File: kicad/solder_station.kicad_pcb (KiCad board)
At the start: 2 copper layers, 25 parts, among them CON1 AVR-ISP-6, IC1 ATMEGA8-P, P1 Weller Connector, Q1 BS170, Q2 IRF4905, U1 LM7805, U2 LM2902N

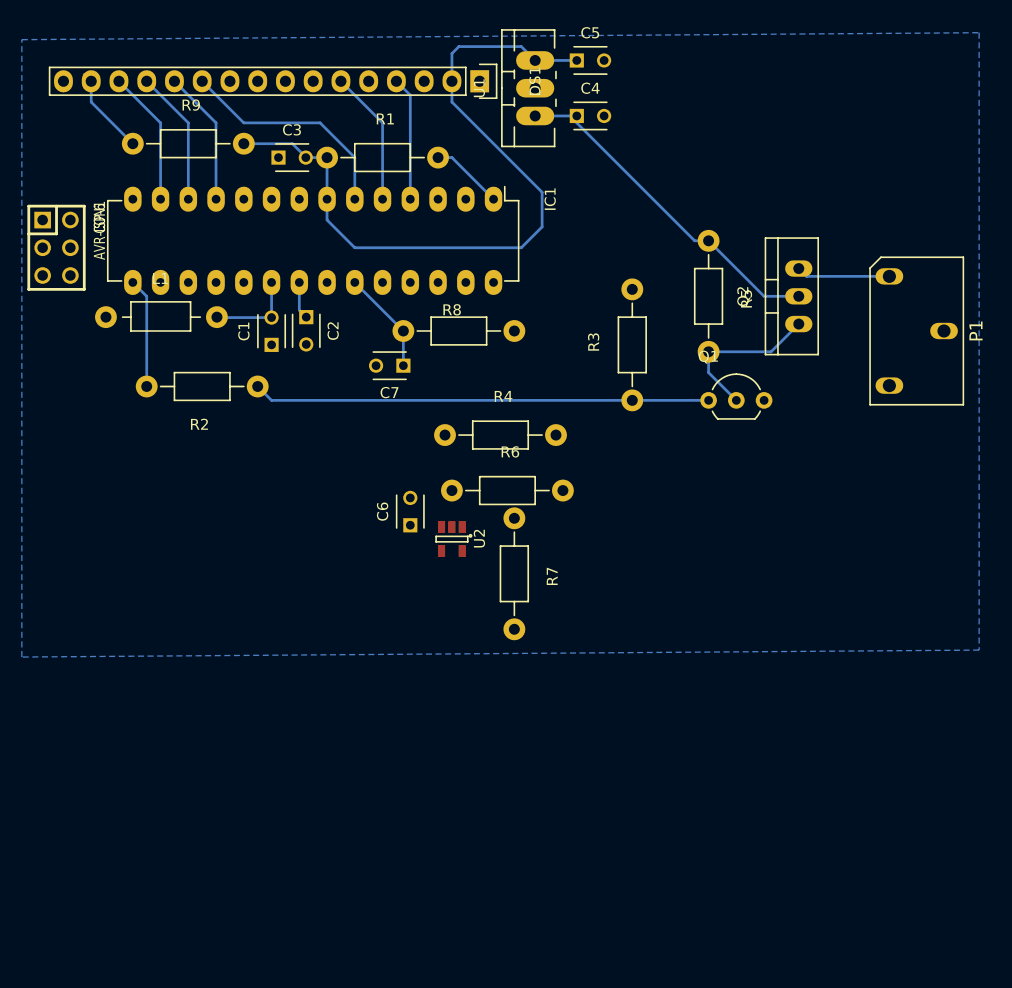
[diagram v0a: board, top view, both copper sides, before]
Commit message: [Kicad] First (bad) version of the PCB.
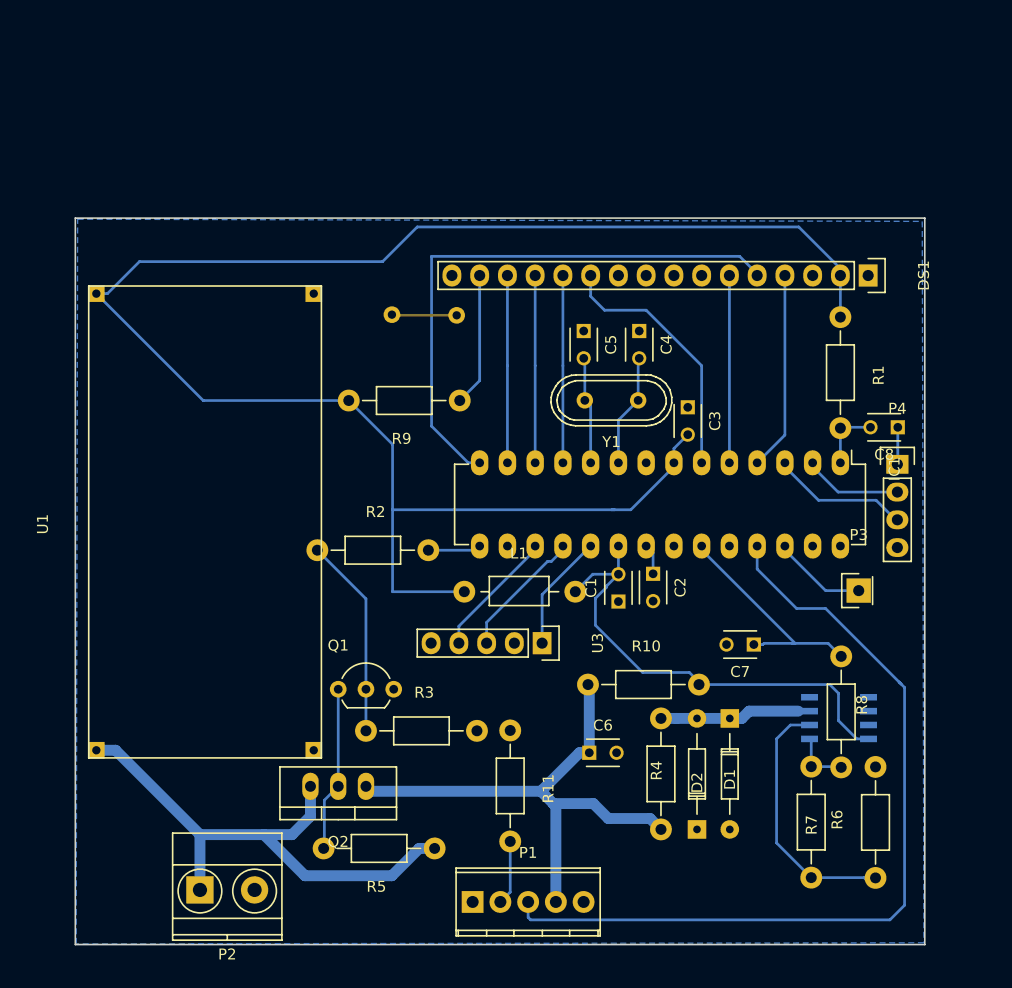
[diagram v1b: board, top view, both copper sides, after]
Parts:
- removed CON1: AVR-ISP-6, connector:CONNECTOR 3 2
- added C8: 100nF, Capacitors_ThroughHole:C_Disc_D3_P2.5, F.Cu at (165.9, 83.1)
- added D1: D, Diodes_ThroughHole:Diode_DO-35_SOD27_Horizontal_RM10, F.Cu at (150.5, 109.8)
- added D2: D, Diodes_ThroughHole:Diode_DO-35_SOD27_Horizontal_RM10, F.Cu at (147.5, 119.9)
- added P2: CONN_01X02, Terminal_Blocks:TerminalBlock_Pheonix_MKDS1.5-2pol, F.Cu at (102.0, 125.5)
- added P3: Standby, Socket_Strips:Socket_Strip_Straight_1x01, F.Cu at (162.3, 98.1)
- added P4: UART, Pin_Headers:Pin_Header_Straight_1x04, F.Cu at (165.9, 86.5)
- added R10: 1MΩ, Resistors_ThroughHole:Resistor_Horizontal_RM10mm, F.Cu at (142.6, 106.7)
- added R11: 1MΩ, Resistors_ThroughHole:Resistor_Horizontal_RM10mm, F.Cu at (130.4, 115.9)
- added REF**1: Pad, my_footprints:Pad, F.Cu at (119.6, 72.8)
- added REF**2: Pad, my_footprints:Pad, F.Cu at (125.5, 72.9)
- added U3: EC11, Pin_Headers:Pin_Header_Straight_1x05, F.Cu at (133.3, 102.9)
- added Y1: 16MHz, Crystals:Crystal_HC49-U_Vertical, F.Cu at (139.7, 80.6)
- C4, C5: value 100nF -> 22pF
- IC1: value ATMEGA8-P -> ATMEGA328-P
- L1: value 10uH -> 10µH
- P1: value Weller Connector -> CONN_01X05; footprint my_footprints:ZIP-3 -> Terminal_Blocks:TerminalBlock_Pheonix_MPT-2.54mm_5pol
- Q1: value BS170 -> 2N7000
- R4: value 1kΩ -> 6.7kΩ
- R5: value R -> 10kΩ
- U1: value LM7805 -> LM2596_module; footprint TO_SOT_Packages_THT:TO-220_Neutral123_Vertical_LargePads -> my_footprints:LM2596
- U2: value LM2902N -> AD8572; footprint TO_SOT_Packages_SMD:SOT-23-5 -> Housings_SOIC:SOIC-8_3.9x4.9mm_Pitch1.27mm; moved to B.Cu
- moved U1 73.7 mm to (91.8, 113.4)
- moved P1 66.2 mm to (127.0, 126.6), turned to 0 degrees
- moved Q2 61.6 mm to (114.7, 116.0), turned to 180 degrees
- moved R5 58.9 mm to (118.4, 121.7), turned to 180 degrees
- moved R8 49.4 mm to (160.7, 109.2), turned to 270 degrees
- moved R1 46.3 mm to (160.7, 78.1), turned to 270 degrees
- moved R6 45.4 mm to (163.9, 119.3), turned to 90 degrees
- moved C3 43.9 mm to (146.7, 81.3), turned to 270 degrees
- moved Q1 43.0 mm to (114.7, 107.1)
- moved L1 41.3 mm to (131.2, 98.2)
- moved C7 41.0 mm to (152.7, 103.0)
- moved R3 40.3 mm to (122.3, 110.9), turned to 0 degrees
- moved IC1 39.9 mm to (160.7, 86.4)
- moved DS1 39.8 mm to (163.2, 69.2)
- moved C1 39.5 mm to (140.3, 99.1)
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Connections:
- net Heater renamed /Heater_PWM
- net LCD_D4 renamed /LCD_D4
- net LCD_D5 renamed /LCD_D5
- net LCD_D6 renamed /LCD_D6
- net LCD_D7 renamed /LCD_D7
- net LCD_RS renamed /LCD_RS
- net LDC_E renamed /LCD_E
- net RESET renamed Net-(C8-Pad2)
- net Temp_sens renamed /Temp_sense
- C4 pad 1: +12V -> GND
- C4 pad 2: GND -> Net-(C4-Pad2)
- C5 pad 1: +5V -> GND
- C5 pad 2: GND -> Net-(C5-Pad2)
- C6 pad 1: Net-(C6-Pad1) -> /Heater+
- DS1 pad 5: GND -> /LCD_RW
- IC1 pad 10: Net-(IC1-Pad10) -> Net-(C5-Pad2)
- IC1 pad 14: Net-(IC1-Pad14) -> /LCD_RW
- IC1 pad 17: MOSI -> /Button_push
- IC1 pad 18: MISO -> /Rotary_B
- IC1 pad 19: SCK -> /Rotary_A
- IC1 pad 2: Net-(IC1-Pad2) -> /RX
- IC1 pad 25: Net-(IC1-Pad25) -> /Button_connected
- IC1 pad 3: Net-(IC1-Pad3) -> /TX
- IC1 pad 9: Net-(IC1-Pad9) -> Net-(C4-Pad2)
- P1 pad 1: Heater_vcc -> GND
- P1 pad 2: Heater_sense -> /Tip
- P1 pad 3: GND -> /Button_connected
- Q2 pad 1: Net-(Q1-Pad2) -> /Heater+
- Q2 pad 2: +12V -> Net-(Q1-Pad1)
- Q2 pad 3: Heater_vcc -> +24V
- R2 pad 1: Net-(Q1-Pad1) -> Net-(Q1-Pad2)
- R3 pad 1: Net-(Q1-Pad1) -> Net-(Q1-Pad2)
- R4 pad 1: Net-(C6-Pad1) -> Net-(D1-Pad1)
- R4 pad 2: Heater_sense -> /Heater+
- R5 pad 1: +12V -> +24V
- R5 pad 2: Net-(Q1-Pad2) -> Net-(Q1-Pad1)
- U1 pad 1: +12V -> +24V
- U2 pad 3: Net-(C6-Pad1) -> Net-(D1-Pad1)
- U2 pad 4: AVcc -> GND
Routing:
- net +5V: track 66.9 -> 161.0 mm
- net /Button_connected: track 0.00 -> 77.2 mm
- net /LCD_RW: track 0.00 -> 52.0 mm
- net /Heater+: track 0.00 -> 50.7 mm
- net +24V: track 0.00 -> 49.5 mm
- net AVcc: track 8.23 -> 44.4 mm
- net +12V: track 31.3 -> 0.00 mm
- net Net-(Q1-Pad1): track 41.8 -> 15.1 mm
- net Net-(R6-Pad1): track 0.00 -> 22.9 mm
- net Net-(D1-Pad1): track 0.00 -> 13.9 mm
- net /TX: track 0.00 -> 12.7 mm
- net /Rotary_B: track 0.00 -> 12.0 mm
- net /Temp_sense: track 9.46 -> 21.3 mm
- net /Button_push: track 0.00 -> 11.8 mm
- net /Rotary_A: track 0.00 -> 11.6 mm
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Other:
- board outline added: 77.8 x 66.5 mm
- net class Default: via_dia 0.6 -> 1.2; via_drill 0.4 -> 0.8
- net class Power added: clearance 0.2, trace_width 1, via_dia 0.6, via_drill 0.4

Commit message: [Kicad] Fix bug in schematics (VGS too high). Still not sure if it is okay this way.
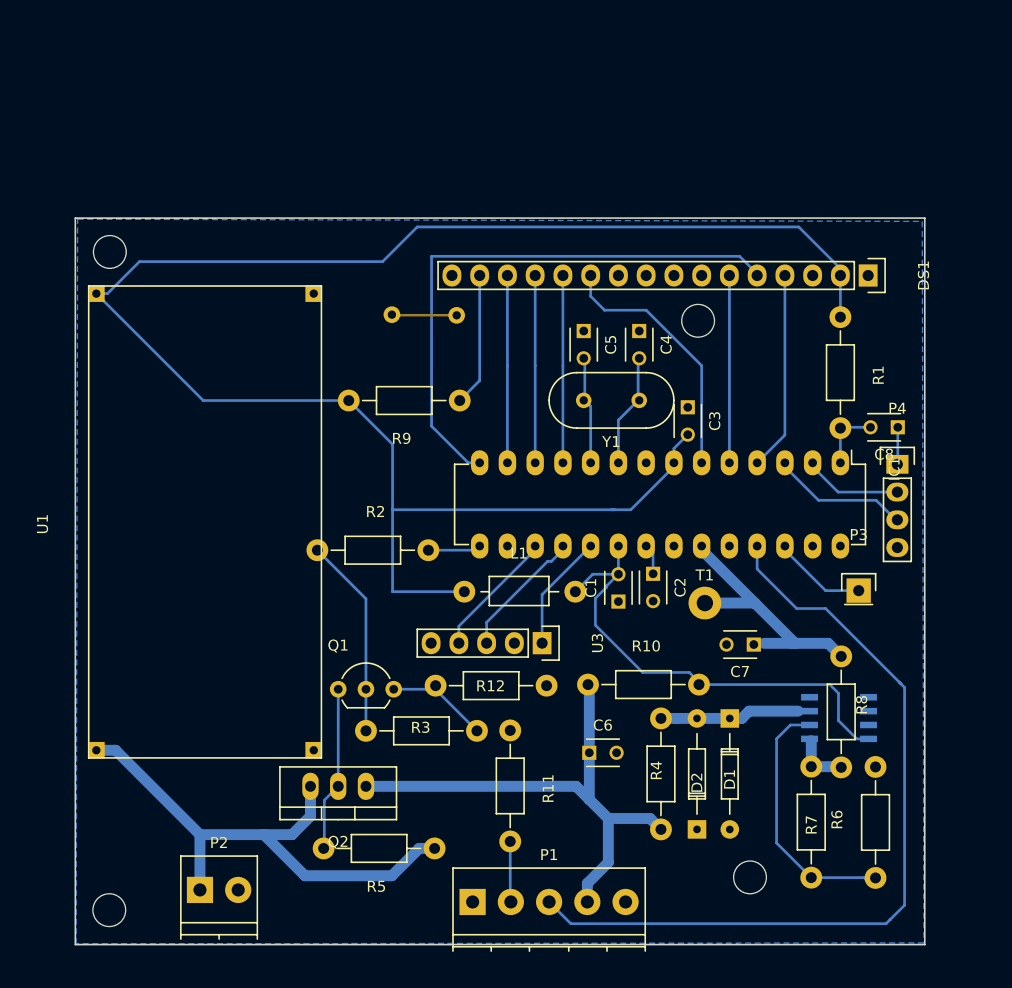
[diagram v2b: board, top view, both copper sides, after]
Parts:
- added Hole1: MountingHole_3mm, Mounting_Holes:MountingHole_3mm, F.Cu at (152.4, 124.3)
- added Hole2: MountingHole_3mm, Mounting_Holes:MountingHole_3mm, F.Cu at (93.7, 127.3)
- added Hole3: MountingHole_3mm, Mounting_Holes:MountingHole_3mm, F.Cu at (93.8, 67.1)
- added Hole4: MountingHole_3mm, Mounting_Holes:MountingHole_3mm, F.Cu at (147.6, 73.4)
- added R12: 10kΩ, Resistors_ThroughHole:Resistor_Horizontal_RM10mm, F.Cu at (128.7, 106.8)
- added T1: Measurement_Point_Round-TH_Big, Measurement_Points:Measurement_Point_Round-TH_Big, F.Cu at (148.2, 99.2)
- P1: footprint Terminal_Blocks:TerminalBlock_Pheonix_MPT-2.54mm_5pol -> Terminal_Blocks:TerminalBlock_Pheonix_PT-3.5mm_5pol
- P2: footprint Terminal_Blocks:TerminalBlock_Pheonix_MKDS1.5-2pol -> Terminal_Blocks:TerminalBlock_Pheonix_PT-3.5mm_2pol
- P3: footprint Socket_Strips:Socket_Strip_Straight_1x01 -> Pin_Headers:Pin_Header_Straight_1x01
- Y1: footprint Crystals:Crystal_HC49-U_Vertical -> Crystals:HC-49V
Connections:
- Q1 pad 3: GND -> Net-(Q1-Pad3)
- R3 pad 2: GND -> Net-(Q1-Pad3)
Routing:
- net Net-(Q1-Pad3): track 0.00 -> 9.67 mm
- net /Temp_sense: track 21.3 -> 26.0 mm
- net /Button_connected: track 77.2 -> 74.8 mm
- net /Heater+: track 50.7 -> 48.5 mm

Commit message: [Kicad] Update schematics. Using ad8551.
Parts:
- removed Hole4: MountingHole_3mm, Mounting_Holes:MountingHole_3mm
- removed T1: Measurement_Point_Round-TH_Big, Measurement_Points:Measurement_Point_Round-TH_Big
- added C9: CP, Capacitors_ThroughHole:C_Radial_D5_L11_P2.5, F.Cu at (112.7, 117.2)
- R10: value 1MΩ -> 300kΩ
- R12, R5: value 10kΩ -> 1kΩ
- R6: value 100Ω -> 1kΩ
- R7: value 50kΩ -> 100kΩ
- moved Q1 16.6 mm to (131.1, 105.2), turned to 180 degrees
- moved Hole3 16.0 mm to (109.7, 67.2)
- moved P2 15.6 mm to (117.5, 123.1)
- moved R6 15.5 mm to (149.0, 114.9), turned to 0 degrees
- moved U2 14.4 mm to (146.8, 105.5)
- moved Hole2 14.1 mm to (107.6, 124.8)
- moved U1 14.1 mm to (105.9, 112.5)
- moved Q2 13.7 mm to (128.2, 114.0), turned to 90 degrees
- moved Hole1 12.9 mm to (165.3, 124.8)
- moved D2 12.1 mm to (153.9, 109.6), turned to 180 degrees
- moved R3 11.8 mm to (111.7, 105.7), turned to 270 degrees
- moved R8 11.1 mm to (152.3, 102.0)
- moved R12 9.33 mm to (121.1, 112.2), turned to 90 degrees
- moved R5 8.76 mm to (118.3, 112.9), turned to 270 degrees
- moved R7 8.24 mm to (156.8, 111.1)
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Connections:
- DS1 pad 10: Net-(DS1-Pad10) -> (no net)
- DS1 pad 7: Net-(DS1-Pad7) -> (no net)
- DS1 pad 8: Net-(DS1-Pad8) -> (no net)
- DS1 pad 9: Net-(DS1-Pad9) -> (no net)
- IC1 pad 16: Net-(IC1-Pad16) -> /Button_push
- IC1 pad 17: /Button_push -> /Rotary_B
- IC1 pad 18: /Rotary_B -> (no net)
- IC1 pad 24: Net-(IC1-Pad24) -> (no net)
- IC1 pad 27: Net-(IC1-Pad27) -> (no net)
- IC1 pad 28: Net-(IC1-Pad28) -> (no net)
- Q1 pad 1: Net-(Q1-Pad1) -> GND
- Q2 pad 1: /Heater+ -> Net-(Q2-Pad1)
- Q2 pad 2: Net-(Q1-Pad1) -> /Heater+
- R12 pad 1: Net-(Q1-Pad3) -> Net-(Q2-Pad1)
- R12 pad 2: GND -> Net-(Q1-Pad3)
- R3 pad 2: Net-(Q1-Pad3) -> GND
- R5 pad 2: Net-(Q1-Pad1) -> Net-(Q2-Pad1)
- U2 pad 1: Net-(R7-Pad1) -> (no net)
- U2 pad 6: (no net) -> Net-(R7-Pad1)
- U2 pad 7: (no net) -> AVcc
- U2 pad 8: AVcc -> (no net)
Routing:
- net /Heater+: track 48.5 -> 25.1 mm
- net +5V: track 161.0 -> 143.6 mm
- net Net-(Q1-Pad1): track 15.1 -> 0.00 mm
- net /Temp_sense: track 26.0 -> 12.1 mm
- net AVcc: track 44.4 -> 30.7 mm
- net /Button_connected: track 74.8 -> 62.4 mm
- net Net-(Q2-Pad1): track 0.00 -> 10.5 mm
- net /Rotary_B: track 12.0 -> 3.24 mm
- net /Button_push: track 11.8 -> 3.24 mm
- net /Rotary_A: track 11.6 -> 3.24 mm
- net /LCD_RW: track 52.0 -> 58.1 mm
- net Net-(R7-Pad1): track 5.47 -> 9.48 mm
- net Net-(Q1-Pad3): track 9.67 -> 5.76 mm
- net /Heater_PWM: track 4.86 -> 8.72 mm
- net Net-(R6-Pad1): track 22.9 -> 26.6 mm
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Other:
- board size 77.8 x 66.5 mm -> 63.8 x 64 mm
- net class Default: clearance 0.2 -> 0.5; trace_width 0.25 -> 0.7
- net class Power: clearance 0.2 -> 0.5
- rule trace_clearance: 0.2 -> 0.5
- rule trace_min: 0.2 -> 0.7
- board text added: "Solder Station V0.1"

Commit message: [Kicad] Update schematics. Use smd capacitors. Add big capacitor for 24V input. Add first approach to fix #1 (still incomplete. Needs testing).
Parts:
- added C10: 100nF, Capacitors_SMD:C_0603_HandSoldering, B.Cu at (115.2, 77.0)
- added L2: 10µH, Choke_Axial_ThroughHole:Choke_Horizontal_RM10mm, F.Cu at (110.2, 77.1)
- C1, C2, C3, C8: footprint Capacitors_ThroughHole:C_Disc_D3_P2.5 -> Capacitors_SMD:C_0603_HandSoldering; moved to B.Cu
- C9: footprint Capacitors_ThroughHole:C_Radial_D5_L11_P2.5 -> Capacitors_ThroughHole:C_Radial_D13_L21_P5
- R1: value 100kΩ -> 10kΩ
- U2: value AD8572 -> AD8551
- moved C7 7.92 mm to (149.0, 97.0)
- moved L1 7.63 mm to (134.8, 100.4)
- moved C1 6.20 mm to (141.0, 96.1), turned to 180 degrees
- moved C9 3.41 mm to (113.0, 120.6), turned to 180 degrees
- moved C3 3.04 mm to (145.2, 83.9), turned to 0 degrees
- moved P2 1.73 mm to (119.2, 123.1)
- moved C2 1.33 mm to (144.8, 96.1), turned to 0 degrees
- moved C8 1.15 mm to (163.8, 88.4), turned to 180 degrees
- moved R10 0.39 mm to (138.2, 108.0)
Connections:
- U1 pad 3: +5V -> Net-(L2-Pad2)
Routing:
- net AVcc: track 30.7 -> 23.7 mm
- net /Temp_sense: track 12.1 -> 6.82 mm
- net Net-(L2-Pad2): track 0.00 -> 4.57 mm
- net Net-(C8-Pad2): track 10.5 -> 6.03 mm
- net +5V: track 143.6 -> 146.4 mm
- net GND: track 4.56 -> 7.29 mm
- net +24V: track 47.1 -> 45.5 mm
